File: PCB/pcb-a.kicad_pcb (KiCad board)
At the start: 2 copper layers, 116.3 x 50.4 mm, 32 parts, among them Q3 BC337, Q4 BC337, SW1 config, U1 MCP23008-xP, U4 ATmega16L-8P

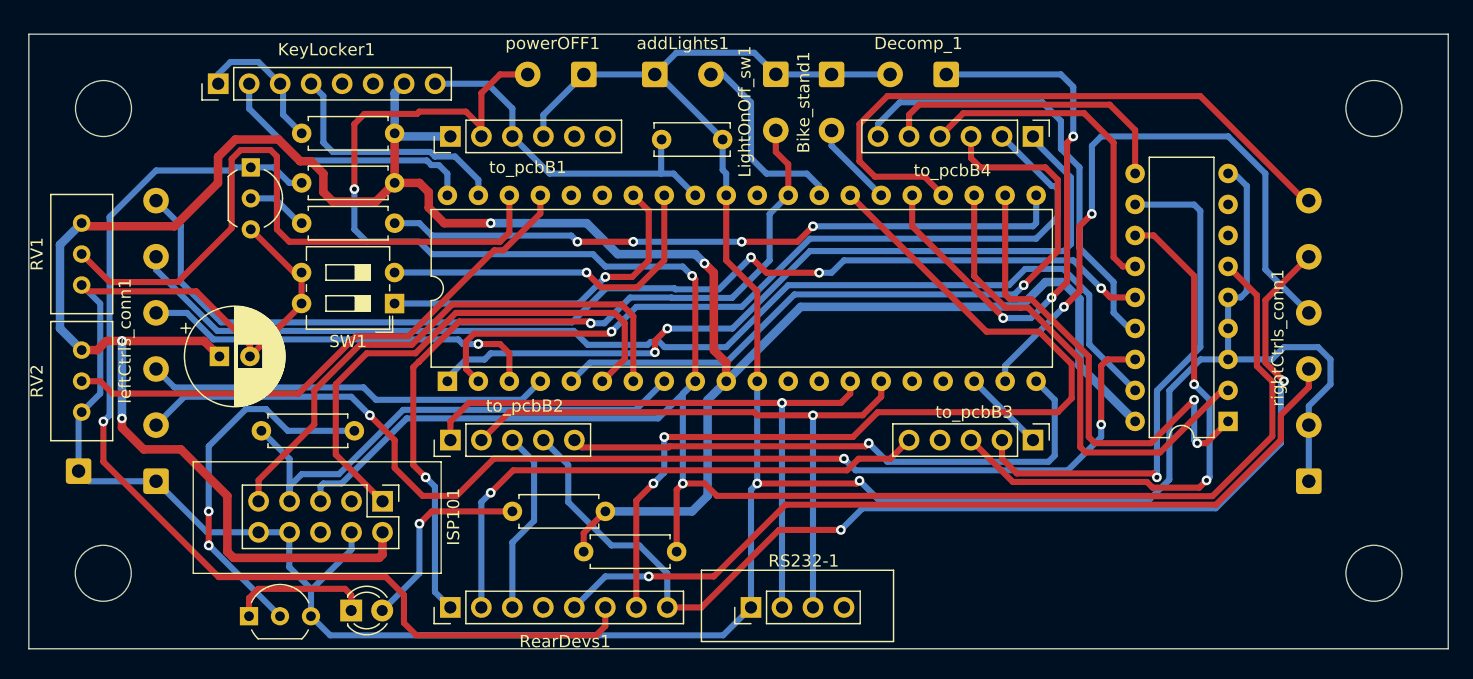
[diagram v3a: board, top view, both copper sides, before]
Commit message: External oscillator
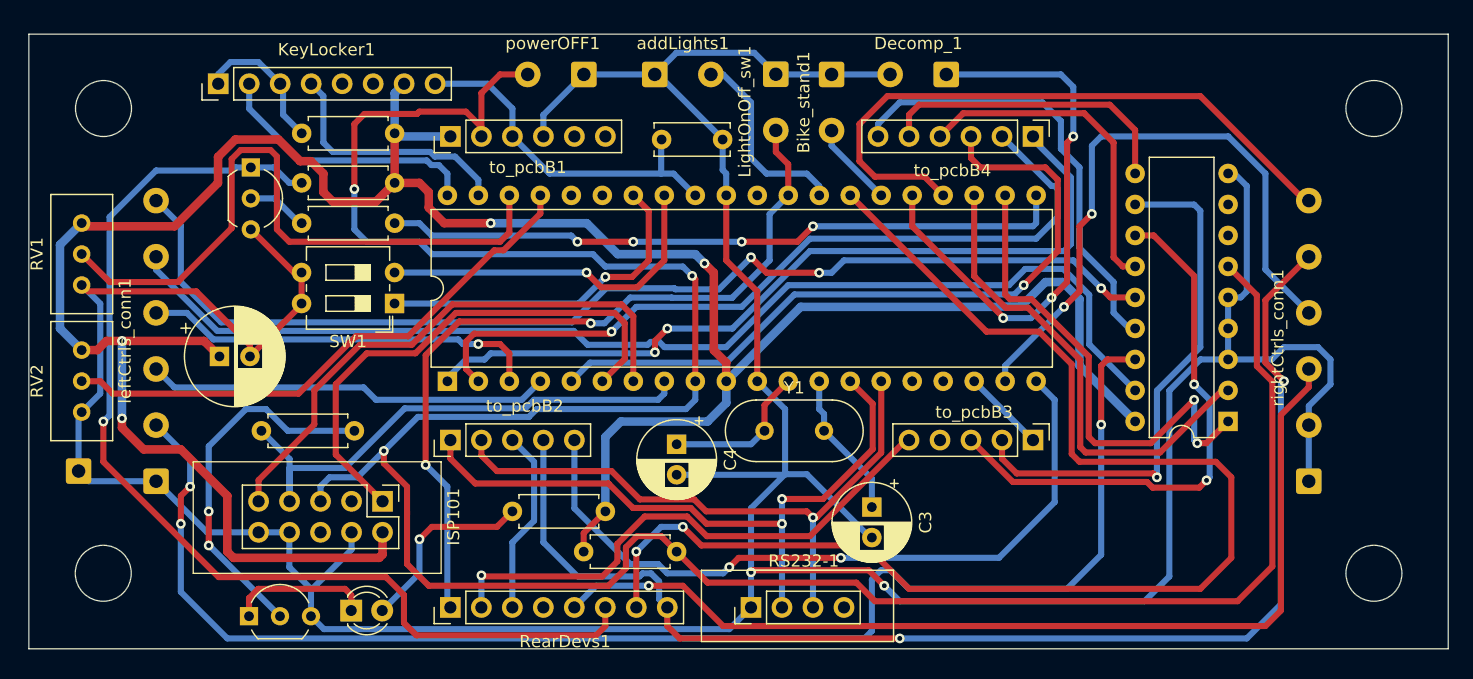
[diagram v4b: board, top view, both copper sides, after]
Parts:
- added C3: 1uF, Capacitor_THT:CP_Radial_D6.3mm_P2.50mm, F.Cu at (168.7, 94.8)
- added C4: 1uF, Capacitor_THT:CP_Radial_D6.3mm_P2.50mm, F.Cu at (152.7, 89.6)
- added Y1: 8Mhz, Crystal:Crystal_HC49-U_Vertical, F.Cu at (159.9, 88.5)
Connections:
- U4 pad 12: unconnected-(U4-Pad12) -> Net-(U4-Pad12)
- U4 pad 13: unconnected-(U4-Pad13) -> Net-(U4-Pad13)
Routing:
- net i_powerOFF: track 183.1 -> 217.3 mm
- net i_neutral: track 76.3 -> 109.1 mm
- net GND: track 284.6 -> 313.5 mm
- net i_leftArrow: track 94.8 -> 117.2 mm
- net c_engineOFF: track 92.6 -> 105.9 mm
- net o_engineON: track 47.3 -> 60.1 mm, vias 1 -> 2
- net Net-(U4-Pad12): track 0.00 -> 12.5 mm
- net Net-(U4-Pad13): track 0.00 -> 12.1 mm
- net c_brakeSwitch: track 70.4 -> 81.3 mm
- net c_RS232_RXD: track 53.0 -> 55.3 mm, vias 1 -> 2
- net Net-(ISP101-Pad7): track 42.2 -> 43.7 mm
- net c_leftArrow: track 45.8 -> 44.5 mm
- net c_rearLight: track 65.6 -> 64.8 mm
- net Net-(D1-Pad2): track 16.4 -> 15.7 mm

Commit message: Wrong capacitors type fixed
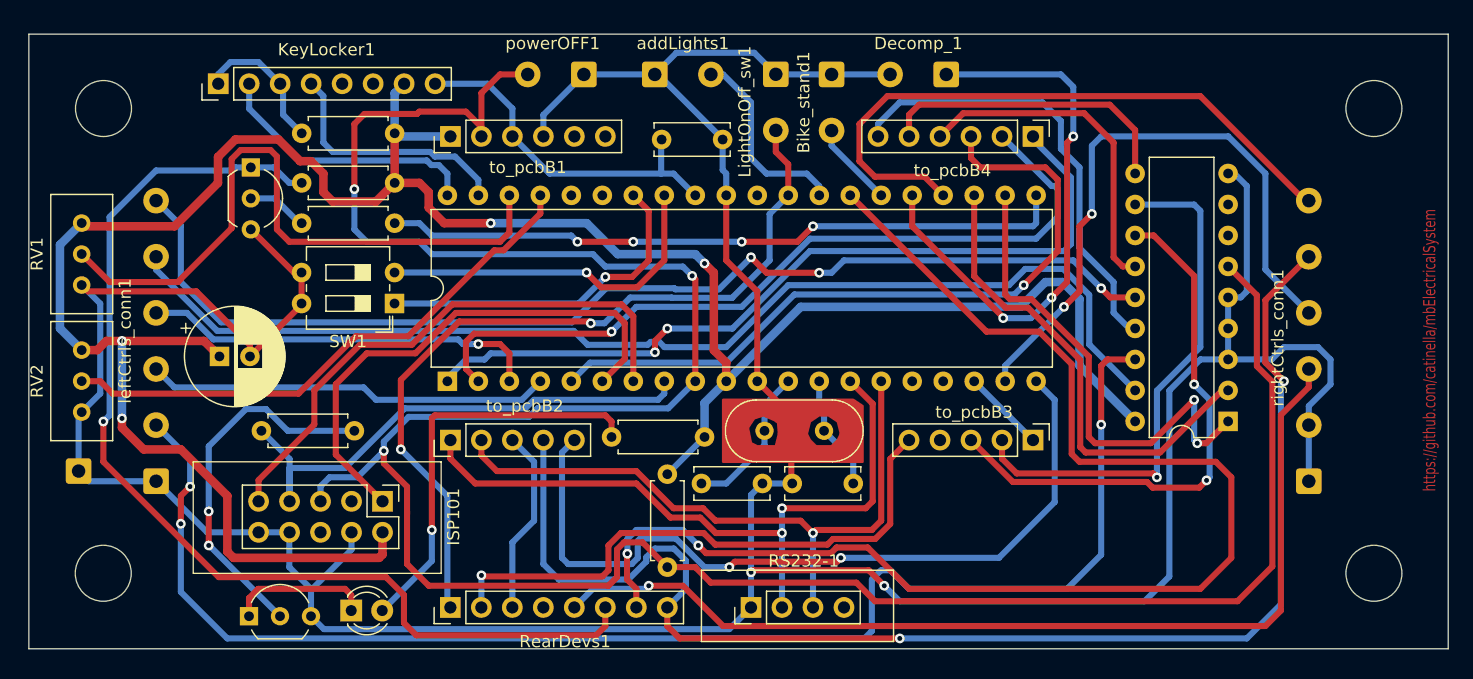
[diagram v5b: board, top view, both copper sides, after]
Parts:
- C3: value 1uF -> 15pf; footprint Capacitor_THT:CP_Radial_D6.3mm_P2.50mm -> Capacitor_THT:C_Disc_D6.0mm_W2.5mm_P5.00mm
- C4: value 1uF -> 15pF; footprint Capacitor_THT:CP_Radial_D6.3mm_P2.50mm -> Capacitor_THT:C_Disc_D6.0mm_W2.5mm_P5.00mm
- moved R9 10.2 mm to (147.3, 89.0)
- moved R2 9.35 mm to (151.9, 92.1), turned to -90 degrees
- moved C4 3.80 mm to (154.7, 92.9), turned to 0 degrees
- moved C3 2.46 mm to (167.1, 92.9), turned to 180 degrees
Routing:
- net Net-(D1-Pad2): track 15.7 -> 33.8 mm
- net GND: track 313.5 -> 296.9 mm
- net tempPower: track 215.3 -> 201.9 mm
- net c_engineOFF: track 105.9 -> 112.6 mm
- net o_engineON: track 60.1 -> 66.1 mm
- net c_RS232_TXT: track 51.6 -> 54.6 mm
- net c_leftArrow: track 44.5 -> 47.4 mm
- net Net-(U4-Pad13): track 12.1 -> 9.54 mm
- net c_RS232_RXD: track 55.3 -> 57.6 mm
- net i_neutral: track 109.1 -> 110.9 mm
- net c_rearLight: track 64.8 -> 66.5 mm
- net i_powerOFF: track 217.3 -> 216.8 mm
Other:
- board text added: "https://github.com/catinella/mbElectricalSystem"

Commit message: Partrial refactoring
Components agregation to find stace for the MAX232 chip
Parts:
- moved U1 6.60 mm to (197.9, 81.2)
- moved C1 3.83 mm to (114.8, 78.6)
- moved Q3 0.25 mm to (117.8, 66.7)
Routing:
- net GND: track 296.9 -> 316.7 mm
- net i_neutral: track 110.9 -> 124.8 mm
- net i_startButton: track 50.9 -> 64.4 mm
- net i_powerOFF: track 216.8 -> 228.1 mm
- net i_engineON: track 52.4 -> 63.2 mm
- net Net-(U1-Pad1): track 40.9 -> 31.3 mm, vias 2 -> 0
- net i_leftArrow: track 117.2 -> 124.4 mm
- net o_leftArrow: track 37.2 -> 31.4 mm
- net o_horn: track 27.5 -> 21.8 mm
- net tempPower: track 201.9 -> 197.4 mm
- net o_rightArrow: track 25.1 -> 21.1 mm
- net o_engineReady: track 43.7 -> 40.8 mm, vias 1 -> 0
- net i_decompr: track 46.7 -> 49.6 mm
- net o_engineON: track 66.1 -> 63.3 mm, vias 2 -> 4
- net i_rightArrow: track 93.3 -> 91.3 mm
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
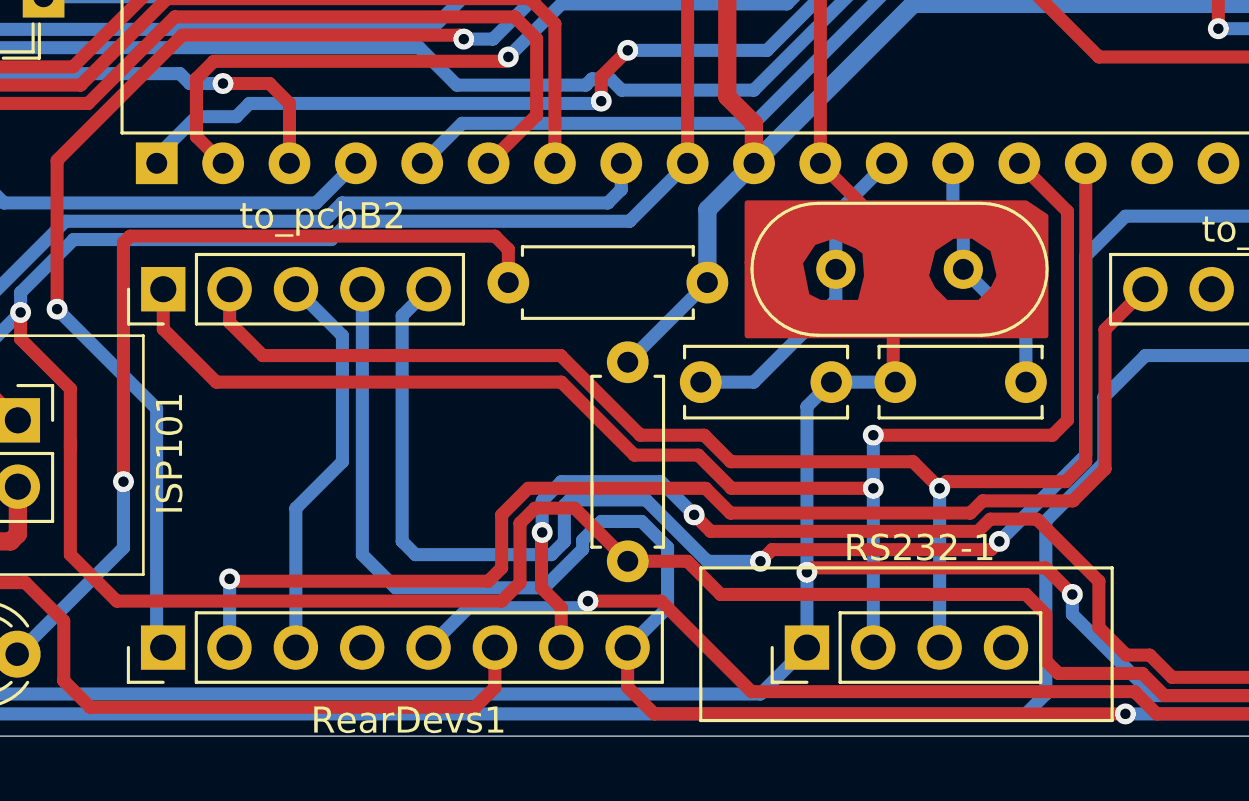
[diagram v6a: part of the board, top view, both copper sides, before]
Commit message: Enhancement: RS232 port
RS232 4-wire connector is compatible with MAX232 driver module
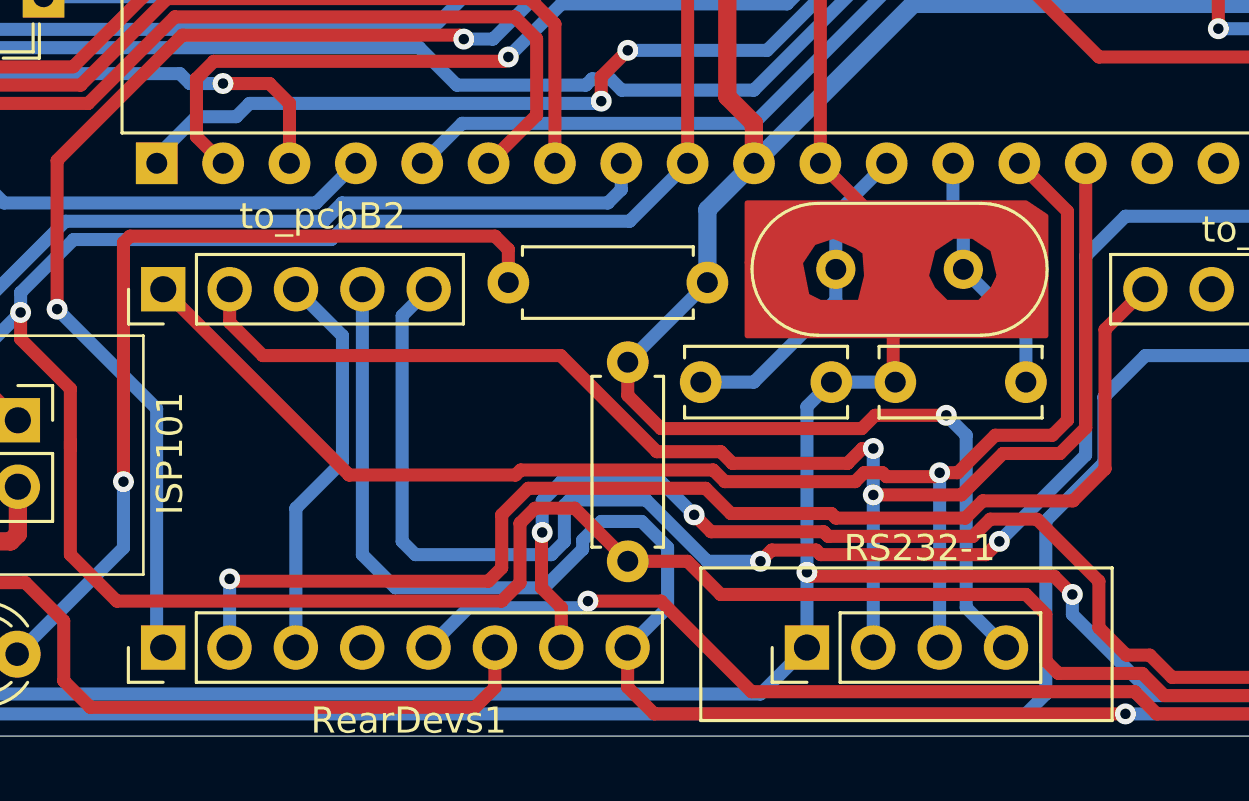
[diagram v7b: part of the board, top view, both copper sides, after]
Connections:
- RS232-1 pad 2: c_RS232_RXD -> c_RS232_TXT
- RS232-1 pad 3: c_RS232_TXT -> c_RS232_RXD
- RS232-1 pad 4: unconnected-(RS232-1-Pad4) -> tempPower
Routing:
- net tempPower: track 197.4 -> 221.5 mm, vias 4 -> 5
- net c_RS232_RXD: track 57.6 -> 56.2 mm, vias 2 -> 1
- net c_RS232_TXT: track 54.6 -> 55.3 mm, vias 1 -> 2

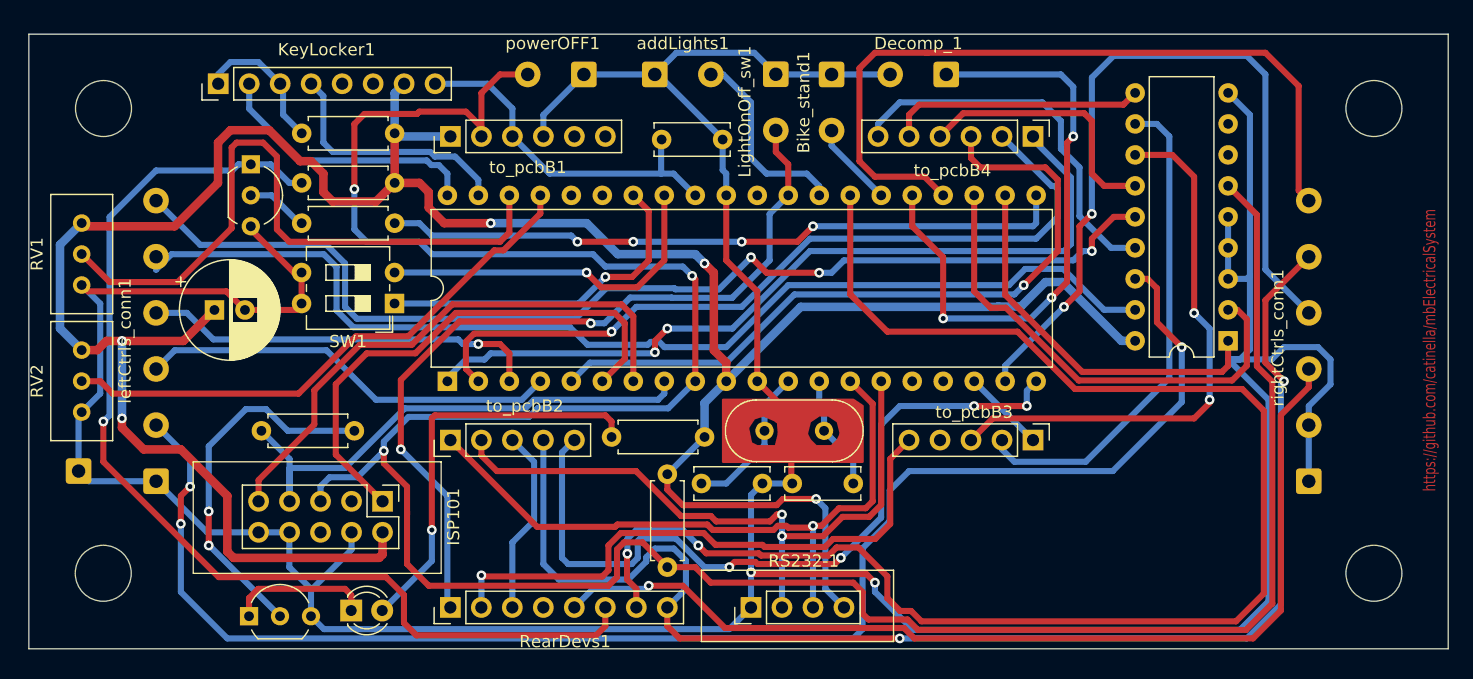
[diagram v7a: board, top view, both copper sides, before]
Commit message: Fixes for analog inputs
- ground reference missed
- AVCC was not connected
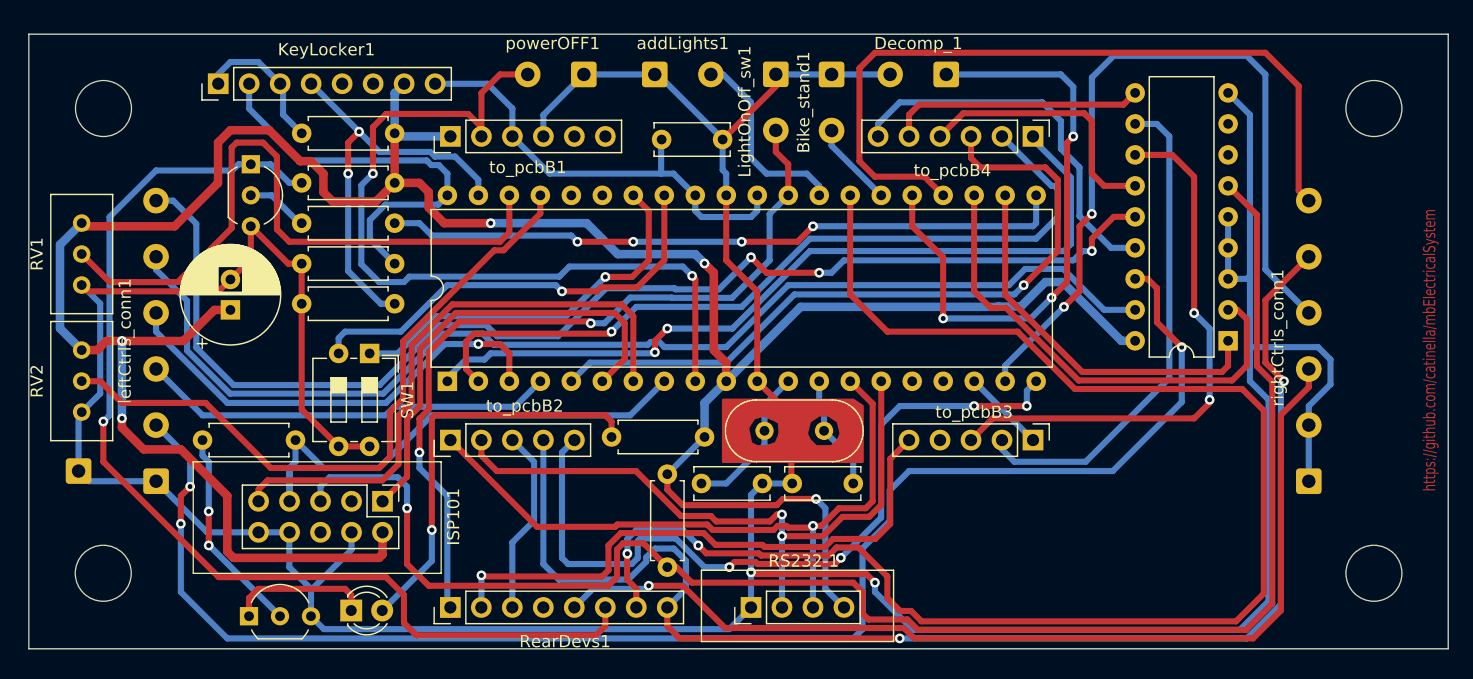
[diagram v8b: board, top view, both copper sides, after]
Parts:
- added R3: 1K, Resistor_THT:R_Axial_DIN0207_L6.3mm_D2.5mm_P7.62mm_Horizontal, F.Cu at (129.5, 74.8)
- added R4: 1K, Resistor_THT:R_Axial_DIN0207_L6.3mm_D2.5mm_P7.62mm_Horizontal, F.Cu at (129.5, 78.1)
- moved R8 12.5 mm to (113.8, 89.3), turned to 0 degrees
- moved SW1 4.57 mm to (127.5, 82.2), turned to -90 degrees
- moved C1 1.31 mm to (116.1, 78.6), turned to 90 degrees
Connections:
- ISP101 pad 5: i_powerOFF -> Net-(ISP101-Pad5)
- R2 pad 2: i_powerOFF -> Net-(ISP101-Pad5)
- U1 pad 6: i_powerOFF -> Net-(ISP101-Pad5)
- U4 pad 30: unconnected-(U4-Pad30) -> +5V
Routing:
- net i_powerOFF: track 228.1 -> 67.5 mm, vias 3 -> 2
- net Net-(ISP101-Pad5): track 0.00 -> 130.6 mm, vias 0 -> 1
- net i_Vx2: track 20.5 -> 35.0 mm, vias 0 -> 2
- net Net-(Q4-Pad2): track 30.3 -> 17.1 mm
- net i_Vx1: track 22.3 -> 33.9 mm
- net Net-(RV2-Pad2): track 45.6 -> 55.6 mm
- net i_horn: track 91.5 -> 100.7 mm
- net +5V: track 29.3 -> 37.3 mm
- net Net-(SW1-Pad2): track 28.9 -> 36.3 mm
- net GND: track 316.6 -> 322.6 mm
- net Net-(ISP101-Pad1): track 43.2 -> 37.7 mm
- net i_upLight: track 32.6 -> 37.5 mm
- net Net-(SW1-Pad1): track 28.2 -> 31.9 mm
- net i_rightArrow: track 91.3 -> 94.7 mm
- net Net-(ISP101-Pad9): track 45.8 -> 48.8 mm
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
